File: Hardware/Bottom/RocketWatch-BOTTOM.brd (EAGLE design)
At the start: 33 x 33 mm, 31 parts, among them U1 AD5242-SO16

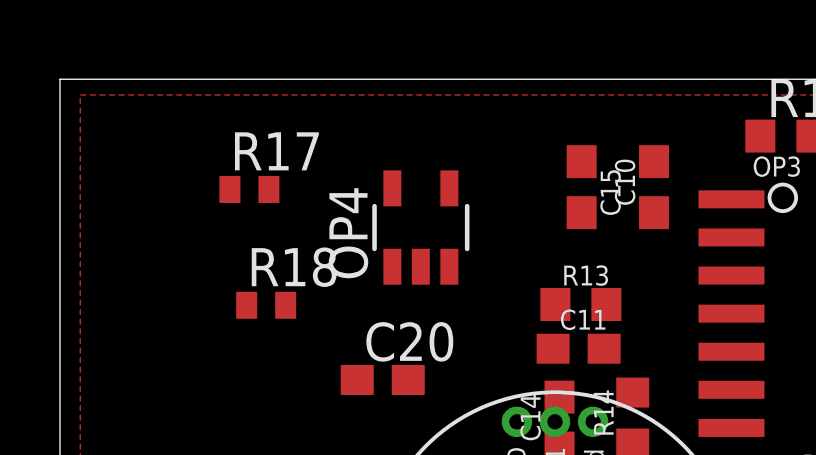
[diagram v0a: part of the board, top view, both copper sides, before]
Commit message: changed schematic and board based on video take 002
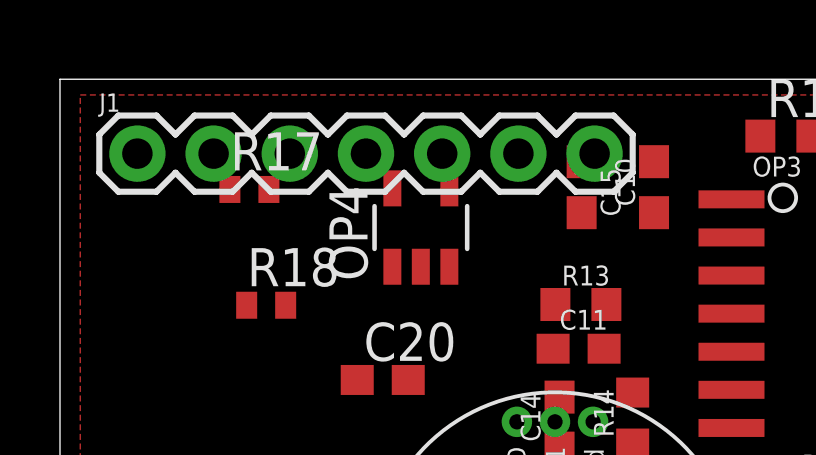
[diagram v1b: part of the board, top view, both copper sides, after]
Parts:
- added J1: (no value), LinnesLab-Connectors:1X07
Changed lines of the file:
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@@
 <attribute name="VALUE" x="2.2098" y="5.7404" size="0.6604" layer="27" rot="R270"/>
+</element>
+<element name="J1" library="LinnesLab-Connectors" package="1X07" value="" x="5.08" y="33.02" smashed="yes">
+<attribute name="NAME" x="3.81" y="34.417" size="0.6096" layer="25" font="vector" ratio="20"/>
+<attribute name="VALUE" x="3.81" y="30.988" size="0.6096" layer="27" font="vector" ratio="20"/>
 </element>
 </elements>

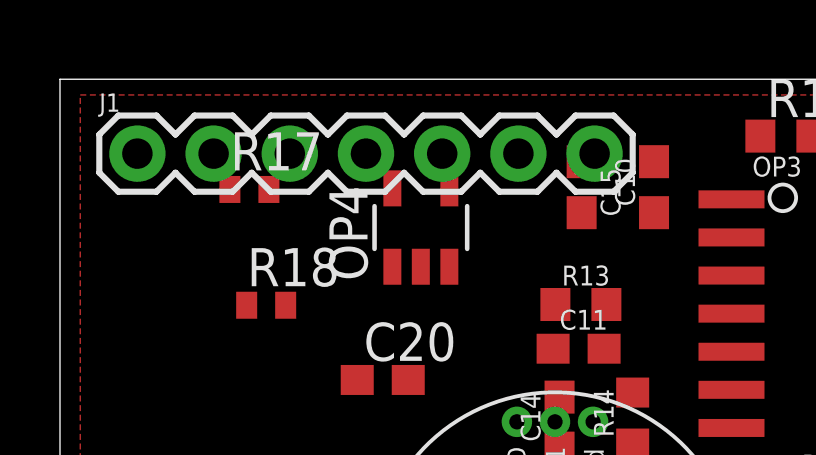
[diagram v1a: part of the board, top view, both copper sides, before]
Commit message: changes to top and bottom board based on take 002 video. Basic schematic and board is complete (no routing done yet)
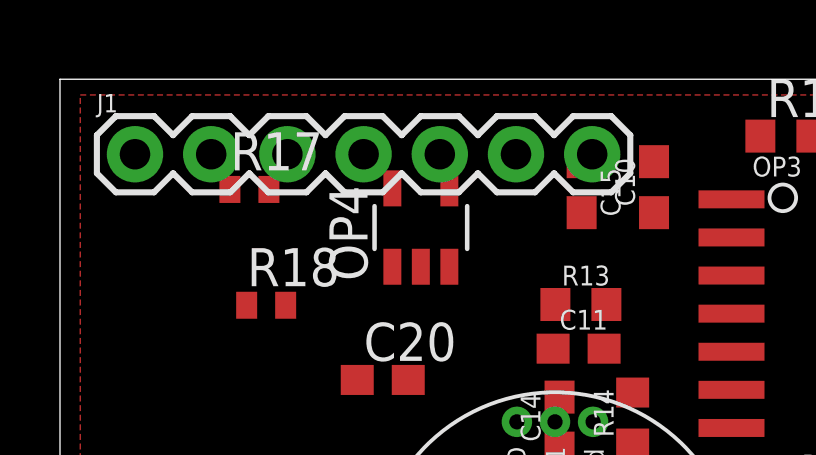
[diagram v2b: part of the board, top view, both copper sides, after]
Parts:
- moved J1 0.08 mm to (5.00, 33.0)
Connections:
- removed net LED.CTRL: U$4.8
- removed net PPG: C21.2, OP3.1, U1.14
- removed net TIA: C10.2, C15.1, OP4.1, U1.3
- new net A6/TIA: C10.2, C15.1, J1.5, OP4.1, U1.3
- new net A7/PPG: C21.2, J1.7, OP3.1, U1.14
- new net D29/LED.CTRL: J1.6, U$4.8
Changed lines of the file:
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@@
 <setting verticaltext="up"/>
 </settings>
-<grid distance="1" unitdist="mil" unit="mil" style="lines" multiple="1" display="no" altdistance="5" altunitdist="mil" altunit="mil"/>
+<grid distance="1" unitdist="mil" unit="mm" style="lines" multiple="1" display="no" altdistance="5" altunitdist="mil" altunit="mil"/>
 <layers>
 <layer number="1" name="Top" color="4" fill="1" visible="yes" active="yes"/>
@@
 <attribute name="VALUE" x="2.2098" y="5.7404" size="0.6604" layer="27" rot="R270"/>
 </element>
-<element name="J1" library="LinnesLab-Connectors" package="1X07" value="" x="5.08" y="33.02" smashed="yes">
-<attribute name="NAME" x="3.81" y="34.417" size="0.6096" layer="25" font="vector" ratio="20"/>
-<attribute name="VALUE" x="3.81" y="30.988" size="0.6096" layer="27" font="vector" ratio="20"/>
+<element name="J1" library="LinnesLab-Connectors" package="1X07" value="" x="5" y="33" smashed="yes">
+<attribute name="NAME" x="3.73" y="34.397" size="0.6096" layer="25" font="vector" ratio="20"/>
+<attribute name="VALUE" x="3.73" y="30.968" size="0.6096" layer="27" font="vector" ratio="20"/>
 </element>
 </elements>
@@
 <wire x1="11.3538" y1="4.0894" x2="18.9934" y2="4.5894" width="0" layer="19" extent="1-1"/>
 </signal>
-<signal name="TIA">
+<signal name="A6/TIA">
 <contactref element="C10" pad="2"/>
 <contactref element="U1" pad="3"/>
 <contactref element="C15" pad="1"/>
 <contactref element="OP4" pad="1"/>
+<contactref element="J1" pad="5"/>
 <wire x1="19.8882" y1="32.7524" x2="22.3012" y2="32.7524" width="0" layer="19" extent="1-1"/>
-<wire x1="13.5788" y1="29.2502" x2="19.8882" y2="32.7524" width="0" layer="19" extent="1-1"/>
+<wire x1="15.16" y1="33" x2="19.8882" y2="32.7524" width="0" layer="19" extent="1-1"/>
+<wire x1="13.5788" y1="29.2502" x2="15.16" y2="33" width="0" layer="19" extent="1-1"/>
 <wire x1="26.6192" y1="10.6426" x2="22.3012" y2="32.7524" width="0" layer="19" extent="1-1"/>
 </signal>
@@
 <wire x1="17.0434" y1="4.5894" x2="17.6934" y2="6.9422" width="0" layer="19" extent="1-1"/>
 </signal>
-<signal name="LED.CTRL">
+<signal name="D29/LED.CTRL">
 <contactref element="U$4" pad="8"/>
+<contactref element="J1" pad="6"/>
+<wire x1="17.0434" y1="6.9422" x2="17.7" y2="33" width="0" layer="19" extent="1-1"/>
 </signal>
 <signal name="N$10">
@@
 <contactref element="U1" pad="1"/>
 </signal>
-<signal name="PPG">
+<signal name="A7/PPG">
 <contactref element="U1" pad="14"/>
 <contactref element="C21" pad="2"/>
 <contactref element="OP3" pad="1"/>
-<wire x1="14.1088" y1="15.3162" x2="24.8828" y2="31.496" width="0" layer="19" extent="1-1"/>
+<contactref element="J1" pad="7"/>
+<wire x1="20.24" y1="33" x2="24.8828" y2="31.496" width="0" layer="19" extent="1-1"/>
+<wire x1="14.1088" y1="15.3162" x2="20.24" y2="33" width="0" layer="19" extent="1-1"/>
 <wire x1="32.766" y1="10.6426" x2="14.1088" y2="15.3162" width="0" layer="19" extent="1-1"/>
 </signal>

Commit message: most of the bottom board routed. Few things left to route and clean up to show all labels.
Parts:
- moved R17 28.8 mm to (31.2, 13.7), turned to 270 degrees
- moved C22 28.6 mm to (30.6, 33.0)
- moved R18 25.1 mm to (30.1, 13.7), turned to 90 degrees
- moved C21 20.8 mm to (32.3, 23.8)
- moved R22 20.8 mm to (25.5, 14.3), turned to 180 degrees
- moved C19 20.0 mm to (25.5, 12.8)
- moved C20 19.9 mm to (33.1, 26.3), turned to 90 degrees
- moved R23 19.9 mm to (25.5, 11.3), turned to 180 degrees
- moved U1 19.3 mm to (11.5, 15.3), turned to 180 degrees
- moved R24 19.0 mm to (31.3, 26.3), turned to 90 degrees
- moved C24 16.7 mm to (8.07, 21.3)
- moved OP4 16.6 mm to (31.1, 29.5), turned to 270 degrees
- moved U$4 15.9 mm to (15.4, 21.5), turned to 270 degrees
- moved R21 14.8 mm to (23.1, 15.6)
- moved C11 10.2 mm to (29.8, 24.5), turned to 270 degrees
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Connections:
- removed net LED: Q1.3
- net LED.C: now also Q1.3
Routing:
- net A7/PPG: track 0.00 -> 52.0 mm, vias 0 -> 4
- net GND: track 0.00 -> 34.0 mm, vias 0 -> 11
- net VREF: track 0.00 -> 24.5 mm, vias 0 -> 4
- net 3.3V: track 0.00 -> 23.4 mm, vias 0 -> 2
- net N$19: track 0.00 -> 22.8 mm
- net PD.C: track 0.00 -> 10.3 mm
- net A6/TIA: track 0.00 -> 9.94 mm
- net N$17: track 0.00 -> 9.62 mm, vias 0 -> 2
- net N$16: track 0.00 -> 8.09 mm
- net N$13: track 0.00 -> 7.80 mm
- net N$15: track 0.00 -> 7.52 mm
- net N$9: track 0.00 -> 6.51 mm
- net N$18: track 0.00 -> 5.91 mm
- net SDA: track 0.00 -> 5.62 mm, vias 0 -> 2
- net SCL: track 0.00 -> 5.33 mm
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- added copper zone on layer 16, net GND

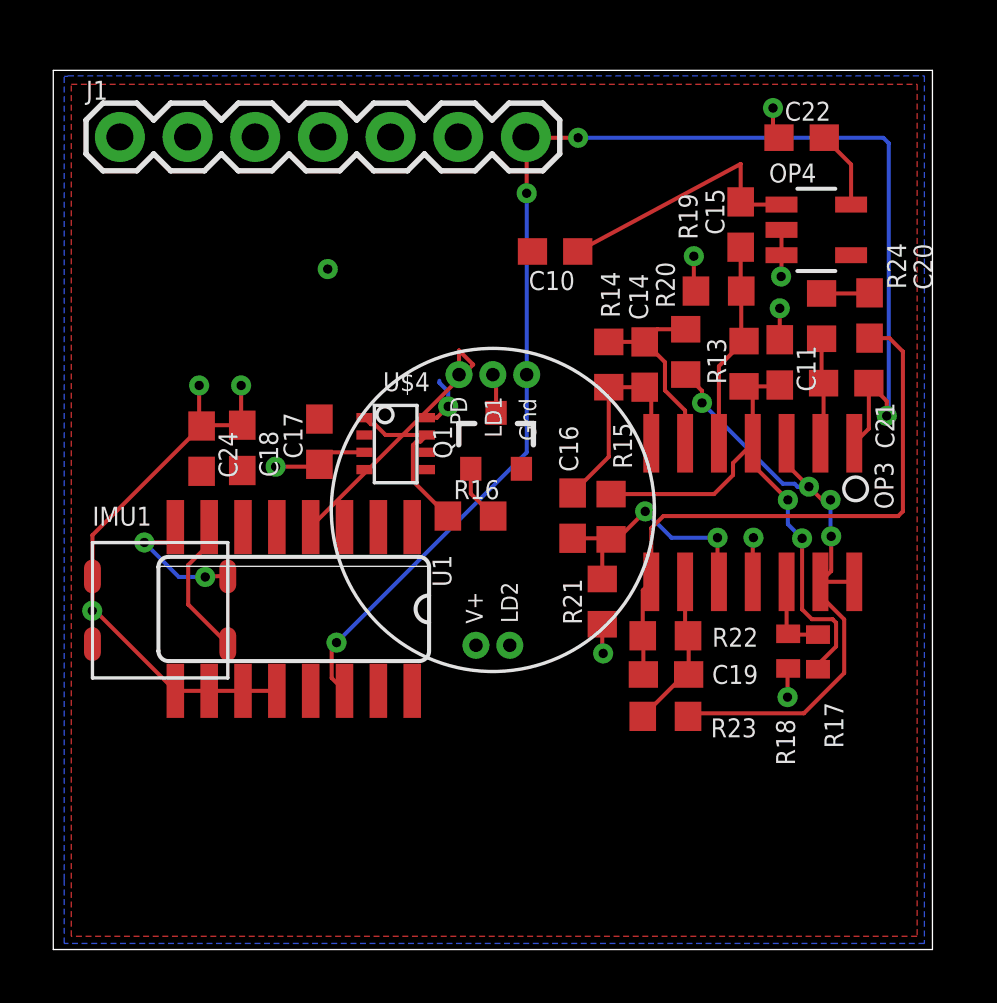
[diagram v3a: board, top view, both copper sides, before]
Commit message: Bottom board wired. DRC had some errors that still need fixed
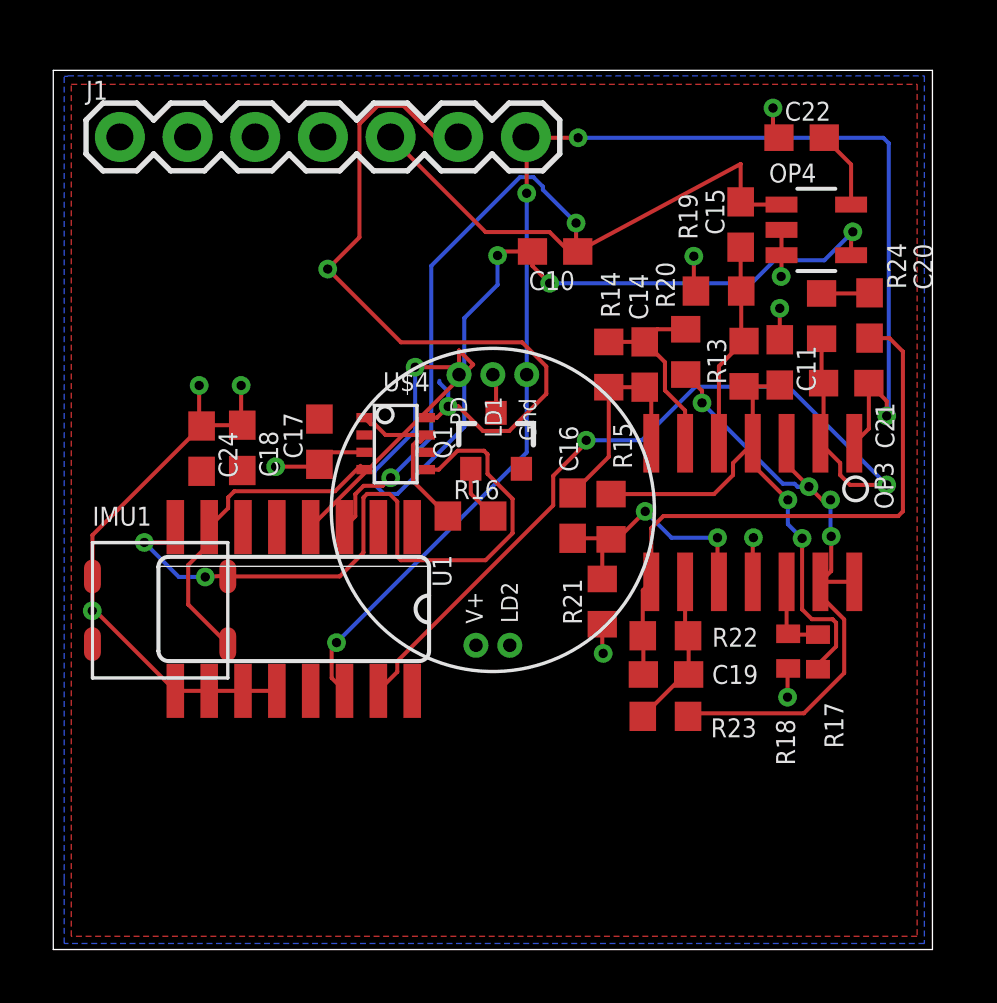
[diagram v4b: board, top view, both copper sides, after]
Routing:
- net PD.C: track 10.3 -> 44.5 mm, vias 0 -> 4
- net G.W2: track 4.00 -> 33.7 mm, vias 0 -> 2
- net A6/TIA: track 9.94 -> 38.9 mm, vias 0 -> 2
- net D29/LED.CTRL: track 2.13 -> 28.0 mm
- net SDA: track 5.62 -> 27.4 mm
- net SCL: track 5.33 -> 12.2 mm
